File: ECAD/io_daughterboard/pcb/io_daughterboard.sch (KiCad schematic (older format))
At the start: 89 parts, among them CON1 BARREL_JACK, P1 CONN_02X32, P10 Slave 5B, P11 Slave 1C, P12 Slave 3C, P13 Slave 4C, P14 Slave 5C, P15 Slave 1D, P16 Slave 3D, P17 Slave 4D, P18 Slave 5D, P19 CONN_01X04, P2 CONN_02X32, P3 Slave 1A, P4 Slave 3A, P5 Slave 4A, P6 Slave 5A, P7 Slave 1B, P8 Slave 3B, P9 Slave 4B, SW1 Reset Button, SW2 User Button, U1 FAN5333BSX, U10 SN74LV1T34DCKR, U11 SN74LV1T34DCKR, U2 SPX3819M5-L-3-3, U3 74HC244, U4 74HC244, U5 74HC244, U6 STMPE811QTR, U7 74HC244, U8 74HC244, U9 74HC244

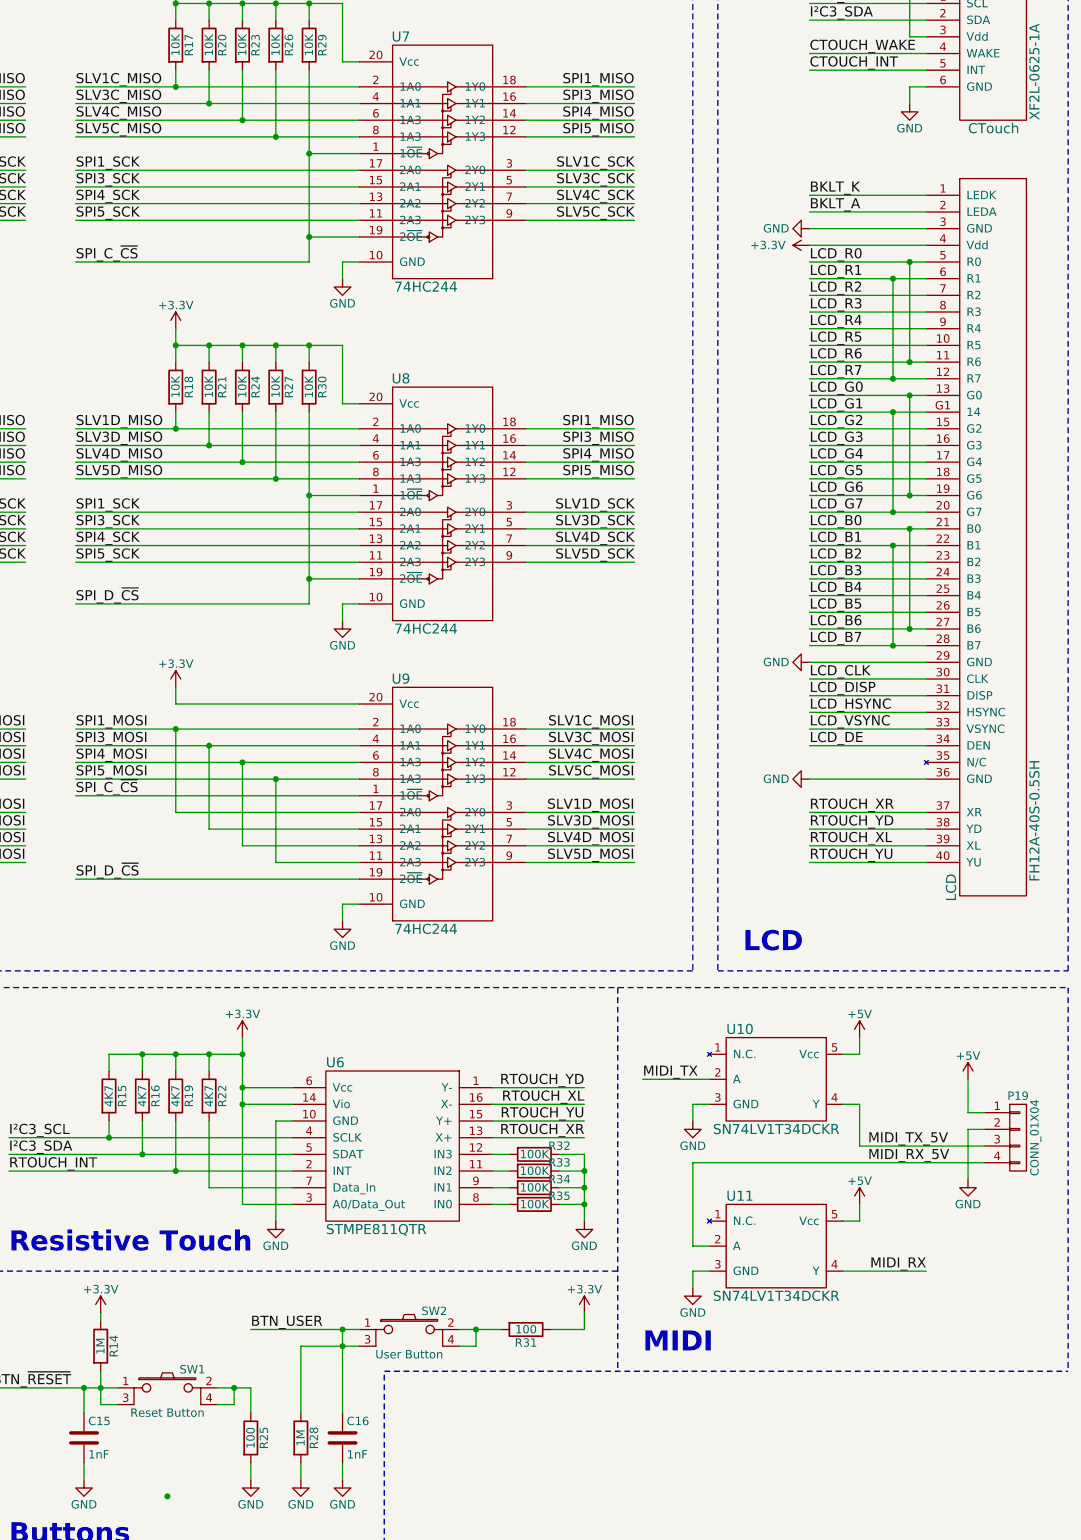
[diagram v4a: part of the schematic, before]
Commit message: PCB and schematic had gotten out of sync.  Now in sync.
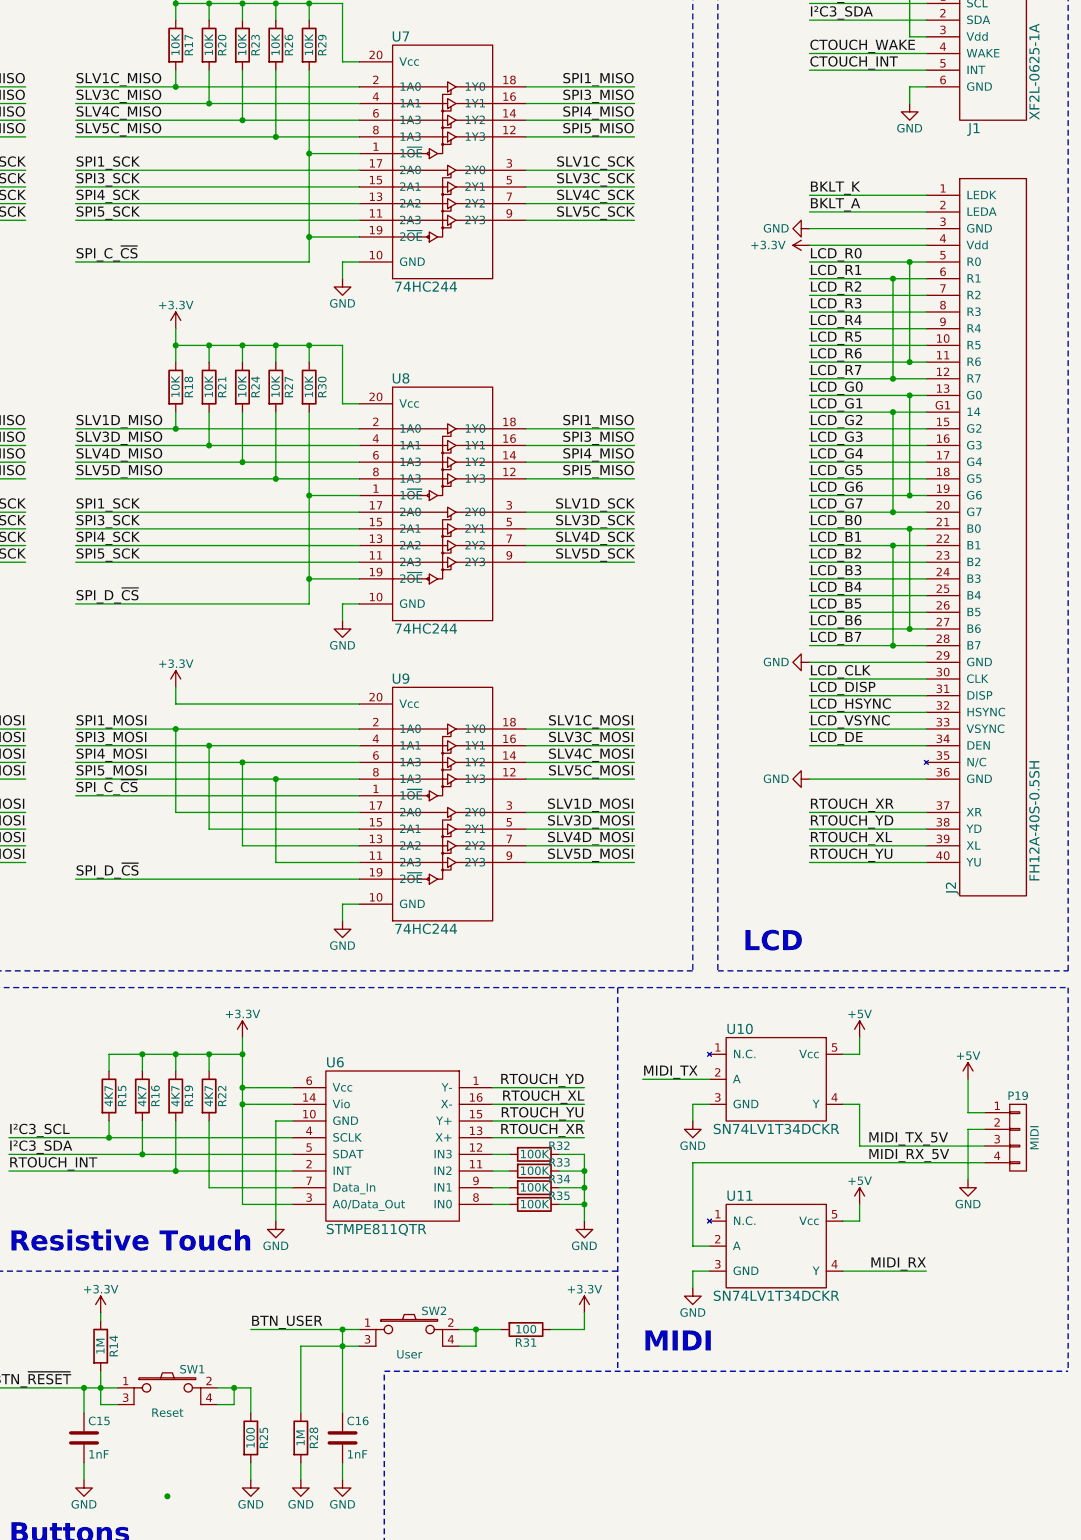
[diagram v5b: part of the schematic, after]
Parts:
- P19: value CONN_01X04 -> MIDI
- R13: footprint Resistors_SMD:R_0603_HandSoldering -> daughterfeet:R_0603_HandSoldering_no_paste
- SW1: value Reset Button -> Reset
- SW2: value User Button -> User
- renumbered CTouch to J1, LCD to J2
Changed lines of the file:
@@
 P 16050 7800
 F 0 "P19" H 16050 8050 50  0000 C CNN
-F 1 "CONN_01X04" V 16150 7800 50  0000 C CNN
+F 1 "MIDI" V 16150 7800 50  0000 C CNN
 F 2 "Connectors_Molex:Molex_PicoBlade_53047-0410_04x1.25mm_Straight" H 16050 7800 50  0001 C CNN
 F 3 "" H 16050 7800 50  0000 C CNN
@@
 $EndComp
 $Comp
-L XF2L-0625-1A CTouch
+L XF2L-0625-1A J1
 U 1 1 5825486E
 P 15750 1300
-F 0 "CTouch" V 15300 1300 60  0000 R CNN
+F 0 "J1" V 15300 1300 60  0000 R CNN
 F 1 "XF2L-0625-1A" H 15350 900 60  0000 L CNN
 F 2 "daughterfeet:XF2L-0625" H 15800 1400 60  0001 C CNN
@@
 $EndComp
 $Comp
-L 4-1734839-0 LCD
+L 4-1734839-0 J2
 U 1 1 58253EA8
 P 15800 4150
-F 0 "LCD" H 13650 4300 60  0000 C CNN
+F 0 "J2" H 13650 4300 60  0000 C CNN
 F 1 "FH12A-40S-0.5SH" H 14050 3800 60  0000 C CNN
 F 2 "daughterfeet:FH12A-40S" H 17050 4200 60  0001 C CNN
@@
 P 12400 8950
 F 0 "SW2" H 12550 9060 50  0000 C CNN
-F 1 "User Button" H 12400 8800 50  0000 C CNN
+F 1 "User" H 12400 8800 50  0000 C CNN
 F 2 "daughterfeet:WS-TASV" H 12400 8950 50  0001 C CNN
 F 3 "" H 12400 8950 50  0000 C CNN
@@
 P 10950 9300
 F 0 "SW1" H 11100 9410 50  0000 C CNN
-F 1 "Reset Button" H 10950 9150 50  0000 C CNN
+F 1 "Reset" H 10950 9150 50  0000 C CNN
 F 2 "daughterfeet:WS-TASV" H 10950 9300 50  0001 C CNN
 F 3 "" H 10950 9300 50  0000 C CNN
@@
 F 0 "R13" V 8680 9550 50  0000 C CNN
 F 1 "N/C" V 8600 9550 50  0000 C CNN
-F 2 "Resistors_SMD:R_0603_HandSoldering" V 8530 9550 50  0001 C CNN
+F 2 "daughterfeet:R_0603_HandSoldering_no_paste" V 8530 9550 50  0001 C CNN
 F 3 "" H 8600 9550 50  0000 C CNN
 	1    8600 9550

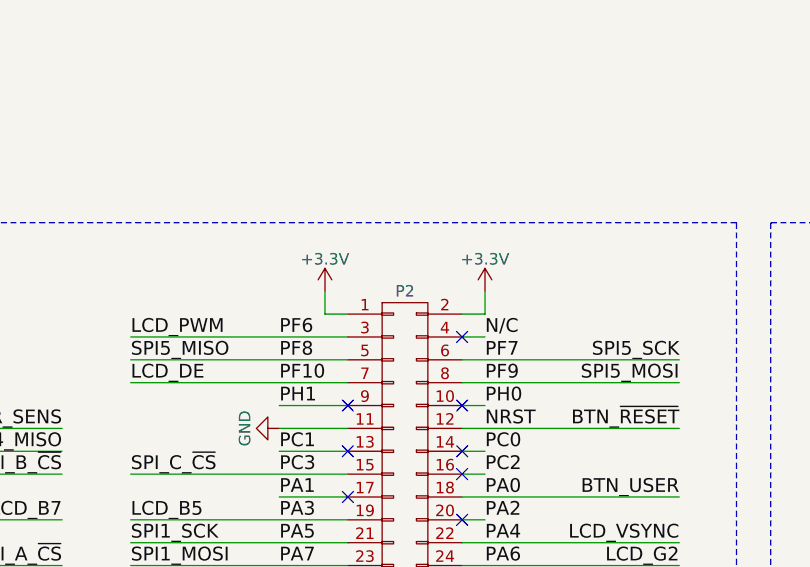
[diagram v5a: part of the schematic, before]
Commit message: Disconnected +3.3V from P2.
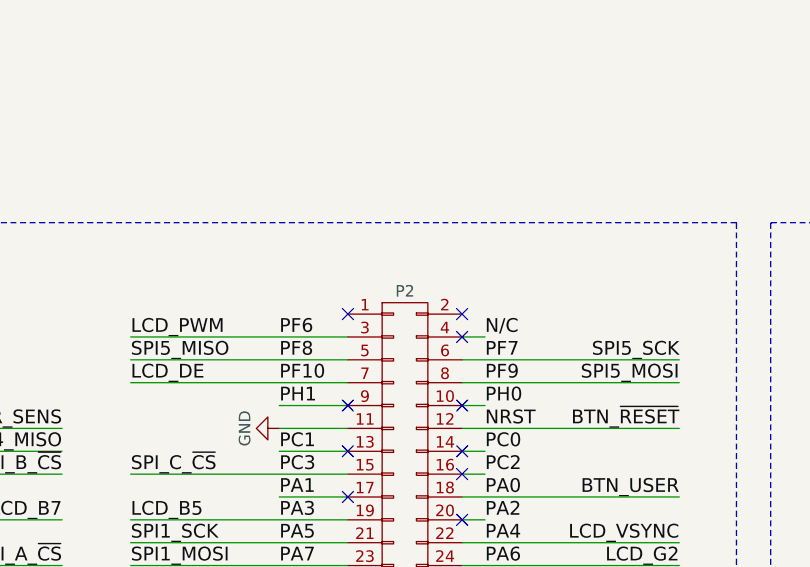
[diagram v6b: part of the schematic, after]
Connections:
- net +3V3: no longer P2.1 (P1), P2.2 (P2)
- no-connect marks 69 -> 71
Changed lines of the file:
@@
 LCD_R7
 NoConn ~ 2200 -2050
-$Comp
-L +3.3V #PWR07
-U 1 1 5827531B
-P 4450 900
-F 0 "#PWR07" H 4450 750 50  0001 C CNN
-F 1 "+3.3V" H 4450 1040 50  0000 C CNN
-F 2 "" H 4450 900 50  0000 C CNN
-F 3 "" H 4450 900 50  0000 C CNN
-	1    4450 900
-	1    0    0    -1
-$EndComp
-$Comp
-L +3.3V #PWR08
-U 1 1 58275392
-P 5150 900
-F 0 "#PWR08" H 5150 750 50  0001 C CNN
-F 1 "+3.3V" H 5150 1040 50  0000 C CNN
-F 2 "" H 5150 900 50  0000 C CNN
-F 3 "" H 5150 900 50  0000 C CNN
-	1    5150 900
-	1    0    0    -1
-$EndComp
 Text Label 4250 1100 0    60   ~ 0
 PF6
@@
 	2450 1000 2350 1000
 Wire Wire Line
-	5150 900  5150 1000
-Wire Wire Line
-	5150 1000 5050 1000
-Wire Wire Line
-	4550 1000 4450 1000
-Wire Wire Line
-	4450 1000 4450 900
-Wire Wire Line
 	4550 1100 3600 1100
 Wire Wire Line
@@
 Connection ~ 7350 7450
 Connection ~ 5350 9450
+NoConn ~ 5050 1000
+NoConn ~ 4550 1000
 $EndSCHEMATC
